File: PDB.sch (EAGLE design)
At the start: 53 parts, among them J1 B06B-HCMKK, J2 B06B-HCMKK, J3 SS-6488-NF-A431, J4 SS-6488-NF-A431, J5 B06B-HCMKK, J6 B03B-HCMKS, J7 B03B-HCMKS, J8 SS-6488-NF-A431

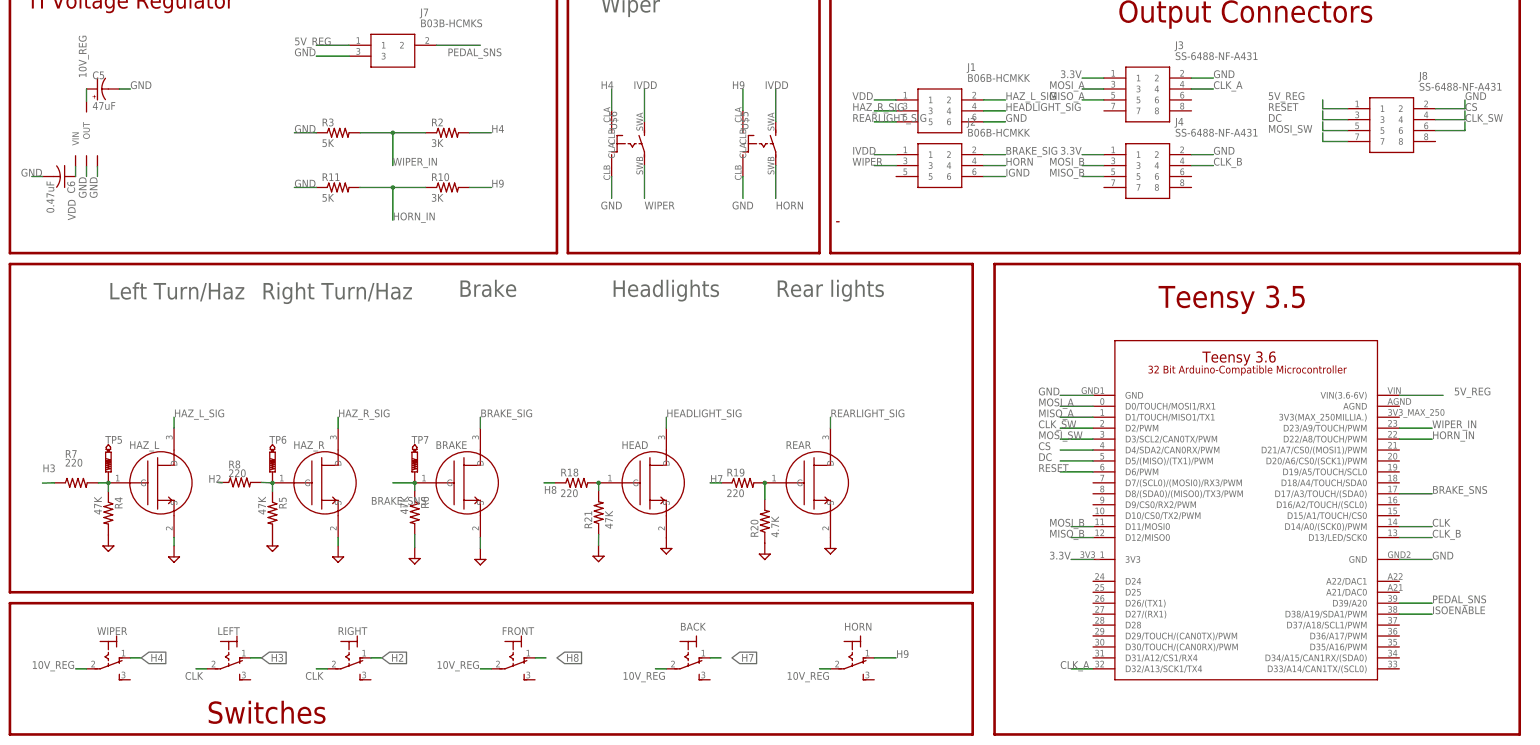
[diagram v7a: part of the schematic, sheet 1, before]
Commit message: With diode, pass signal direcely to ISOENABLE
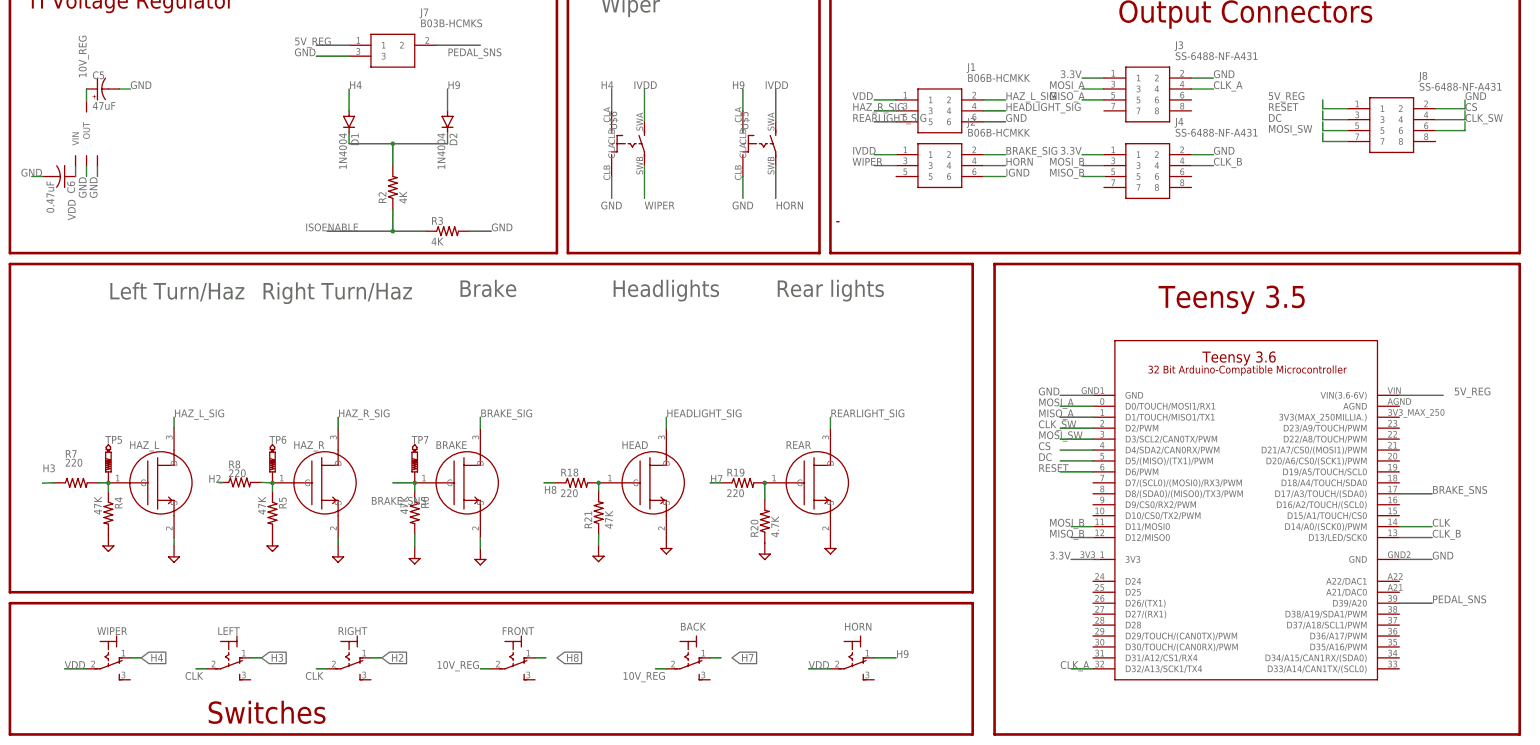
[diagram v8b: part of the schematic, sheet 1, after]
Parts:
- removed R10: 3K, master_library:R-US_R0805
- removed R11: 5K, master_library:R-US_R0805
- added D1, D2: 1N4004, diode:1N4004
- R2: value 3K -> 4K
- R3: value 5K -> 4K
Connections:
- removed net HORN_IN: R10.1, R11.2, U$3.D22/A8/TOUCH/PWM
- removed net WIPER_IN: R2.1, R3.2, U$3.D23/A9/TOUCH/PWM
- new net N$3: D1.C, D2.C, R2.2
- net 10V_REG: no longer HORN.P, WIPER.P
- net GND: now also R3.2; no longer R11.1, R3.1
- net H4: now also D1.A; no longer R2.2
- net H9: now also D2.A; no longer R10.2
- net ISOENABLE: now also R2.1, R3.1; no longer U$3.D38/A19/SDA1/PWM
- net VDD: now also HORN.P, WIPER.P
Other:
- moved on the sheet: R2, R3
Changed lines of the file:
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@@
 <part name="U$6" library="AUX Lib" deviceset="TE_CON_OJE-SH-112DM,095\" device=""/>
 <part name="J8" library="AUX Lib" deviceset="SS-6488-NF-A431" device=""/>
-<part name="R2" library="master_library" deviceset="R-US_" device="R0805" package3d_urn="urn:adsk.eagle:package:2274104/1" value="3K"/>
-<part name="R3" library="master_library" deviceset="R-US_" device="R0805" package3d_urn="urn:adsk.eagle:package:2274104/1" value="5K"/>
-<part name="R10" library="master_library" deviceset="R-US_" device="R0805" package3d_urn="urn:adsk.eagle:package:2274104/1" value="3K"/>
-<part name="R11" library="master_library" deviceset="R-US_" device="R0805" package3d_urn="urn:adsk.eagle:package:2274104/1" value="5K"/>
+<part name="D1" library="diode" library_urn="urn:adsk.eagle:library:210" deviceset="1N4004" device="" package3d_urn="urn:adsk.eagle:package:43336/1"/>
+<part name="D2" library="diode" library_urn="urn:adsk.eagle:library:210" deviceset="1N4004" device="" package3d_urn="urn:adsk.eagle:package:43336/1"/>
+<part name="R2" library="master_library" deviceset="R-US_" device="R0805" package3d_urn="urn:adsk.eagle:package:2274104/1" value="4K"/>
+<part name="R3" library="master_library" deviceset="R-US_" device="R0805" package3d_urn="urn:adsk.eagle:package:2274104/1" value="4K"/>
 </parts>
 <sheets>
@@
 <attribute name="VALUE" x="223.012" y="119.888" size="1.778" layer="96" align="center-left"/>
 </instance>
-<instance part="R2" gate="G$1" x="-2.54" y="109.22" smashed="yes">
-<attribute name="NAME" x="-6.35" y="110.7186" size="1.778" layer="95"/>
-<attribute name="VALUE" x="-6.35" y="105.918" size="1.778" layer="96"/>
-</instance>
-<instance part="R3" gate="G$1" x="-27.94" y="109.22" smashed="yes">
-<attribute name="NAME" x="-31.75" y="110.7186" size="1.778" layer="95"/>
-<attribute name="VALUE" x="-31.75" y="105.918" size="1.778" layer="96"/>
-</instance>
-<instance part="R10" gate="G$1" x="-2.54" y="96.52" smashed="yes">
-<attribute name="NAME" x="-6.35" y="98.0186" size="1.778" layer="95"/>
-<attribute name="VALUE" x="-6.35" y="93.218" size="1.778" layer="96"/>
-</instance>
-<instance part="R11" gate="G$1" x="-27.94" y="96.52" smashed="yes">
-<attribute name="NAME" x="-31.75" y="98.0186" size="1.778" layer="95"/>
-<attribute name="VALUE" x="-31.75" y="93.218" size="1.778" layer="96"/>
+<instance part="D1" gate="1" x="-25.4" y="111.76" smashed="yes" rot="R270">
+<attribute name="NAME" x="-24.9174" y="109.22" size="1.778" layer="95" rot="R270"/>
+<attribute name="VALUE" x="-27.7114" y="109.22" size="1.778" layer="96" rot="R270"/>
+</instance>
+<instance part="D2" gate="1" x="-2.54" y="111.76" smashed="yes" rot="R270">
+<attribute name="NAME" x="-2.0574" y="109.22" size="1.778" layer="95" rot="R270"/>
+<attribute name="VALUE" x="-4.8514" y="109.22" size="1.778" layer="96" rot="R270"/>
+</instance>
+<instance part="R2" gate="G$1" x="-15.24" y="96.52" smashed="yes" rot="R90">
+<attribute name="NAME" x="-16.7386" y="92.71" size="1.778" layer="95" rot="R90"/>
+<attribute name="VALUE" x="-11.938" y="92.71" size="1.778" layer="96" rot="R90"/>
+</instance>
+<instance part="R3" gate="G$1" x="-2.54" y="86.36" smashed="yes">
+<attribute name="NAME" x="-6.35" y="87.8586" size="1.778" layer="95"/>
+<attribute name="VALUE" x="-6.35" y="83.058" size="1.778" layer="96"/>
 </instance>
 </instances>
@@
 <label x="91.44" y="116.84" size="1.778" layer="95"/>
 </segment>
+<segment>
+<pinref part="WIPER" gate="1" pin="P"/>
+<wire x1="-86.36" y1="-15.24" x2="-91.44" y2="-15.24" width="0.1524" layer="91"/>
+<label x="-91.44" y="-15.24" size="1.778" layer="95"/>
+</segment>
+<segment>
+<pinref part="HORN" gate="1" pin="P"/>
+<wire x1="86.36" y1="-15.24" x2="81.28" y2="-15.24" width="0.1524" layer="91"/>
+<label x="81.28" y="-15.24" size="1.778" layer="95"/>
+</segment>
 </net>
 <net name="HAZ_L_SIG" class="0">
@@
 </segment>
 <segment>
-<pinref part="R2" gate="G$1" pin="2"/>
-<wire x1="2.54" y1="109.22" x2="7.62" y2="109.22" width="0.1524" layer="91"/>
-<label x="7.62" y="109.22" size="1.778" layer="95"/>
+<pinref part="D1" gate="1" pin="A"/>
+<wire x1="-25.4" y1="114.3" x2="-25.4" y2="119.38" width="0.1524" layer="91"/>
+<label x="-25.4" y="119.38" size="1.778" layer="95"/>
 </segment>
 </net>
@@
 </segment>
 <segment>
-<pinref part="WIPER" gate="1" pin="P"/>
-<wire x1="-86.36" y1="-15.24" x2="-88.9" y2="-15.24" width="0.1524" layer="91"/>
-<label x="-99.06" y="-15.24" size="1.778" layer="95"/>
-</segment>
-<segment>
 <pinref part="FRONT" gate="1" pin="P"/>
 <wire x1="7.62" y1="-15.24" x2="5.08" y2="-15.24" width="0.1524" layer="91"/>
@@
 <wire x1="48.26" y1="-15.24" x2="45.72" y2="-15.24" width="0.1524" layer="91"/>
 <label x="38.1" y="-17.78" size="1.778" layer="95"/>
-</segment>
-<segment>
-<pinref part="HORN" gate="1" pin="P"/>
-<wire x1="86.36" y1="-15.24" x2="83.82" y2="-15.24" width="0.1524" layer="91"/>
-<label x="76.2" y="-17.78" size="1.778" layer="95"/>
 </segment>
 </net>
@@
 </segment>
 <segment>
-<pinref part="R3" gate="G$1" pin="1"/>
-<wire x1="-33.02" y1="109.22" x2="-38.1" y2="109.22" width="0.1524" layer="91"/>
-<label x="-38.1" y="109.22" size="1.778" layer="95"/>
-</segment>
-<segment>
-<pinref part="R11" gate="G$1" pin="1"/>
-<wire x1="-33.02" y1="96.52" x2="-38.1" y2="96.52" width="0.1524" layer="91"/>
-<label x="-38.1" y="96.52" size="1.778" layer="95"/>
+<pinref part="R3" gate="G$1" pin="2"/>
+<wire x1="2.54" y1="86.36" x2="7.62" y2="86.36" width="0.1524" layer="91"/>
+<label x="7.62" y="86.36" size="1.778" layer="95"/>
 </segment>
 </net>
@@
 </segment>
 <segment>
-<pinref part="U$3" gate="G$1" pin="D38/A19/SDA1/PWM"/>
-<wire x1="218.44" y1="-2.54" x2="226.06" y2="-2.54" width="0.1524" layer="91"/>
-<label x="226.06" y="-2.54" size="1.778" layer="95"/>
+<pinref part="R2" gate="G$1" pin="1"/>
+<wire x1="-15.24" y1="91.44" x2="-15.24" y2="86.36" width="0.1524" layer="91"/>
+<wire x1="-15.24" y1="86.36" x2="-7.62" y2="86.36" width="0.1524" layer="91"/>
+<pinref part="R3" gate="G$1" pin="1"/>
+<wire x1="-15.24" y1="86.36" x2="-30.48" y2="86.36" width="0.1524" layer="91"/>
+<junction x="-15.24" y="86.36"/>
+<label x="-35.56" y="86.36" size="1.778" layer="95"/>
 </segment>
 </net>
@@
 </segment>
 <segment>
-<pinref part="R10" gate="G$1" pin="2"/>
-<wire x1="2.54" y1="96.52" x2="7.62" y2="96.52" width="0.1524" layer="91"/>
-<label x="7.62" y="96.52" size="1.778" layer="95"/>
+<pinref part="D2" gate="1" pin="A"/>
+<wire x1="-2.54" y1="114.3" x2="-2.54" y2="119.38" width="0.1524" layer="91"/>
+<label x="-2.54" y="119.38" size="1.778" layer="95"/>
 </segment>
 </net>
@@
 </segment>
 </net>
-<net name="WIPER_IN" class="0">
-<segment>
-<pinref part="U$3" gate="G$1" pin="D23/A9/TOUCH/PWM"/>
-<wire x1="218.44" y1="40.64" x2="226.06" y2="40.64" width="0.1524" layer="91"/>
-<label x="226.06" y="40.64" size="1.778" layer="95"/>
-</segment>
-<segment>
-<pinref part="R2" gate="G$1" pin="1"/>
-<pinref part="R3" gate="G$1" pin="2"/>
-<wire x1="-7.62" y1="109.22" x2="-15.24" y2="109.22" width="0.1524" layer="91"/>
-<wire x1="-15.24" y1="109.22" x2="-22.86" y2="109.22" width="0.1524" layer="91"/>
-<wire x1="-15.24" y1="109.22" x2="-15.24" y2="101.6" width="0.1524" layer="91"/>
-<junction x="-15.24" y="109.22"/>
-<label x="-15.24" y="101.6" size="1.778" layer="95"/>
-</segment>
-</net>
-<net name="HORN_IN" class="0">
-<segment>
-<pinref part="U$3" gate="G$1" pin="D22/A8/TOUCH/PWM"/>
-<wire x1="218.44" y1="38.1" x2="226.06" y2="38.1" width="0.1524" layer="91"/>
-<label x="226.06" y="38.1" size="1.778" layer="95"/>
-</segment>
-<segment>
-<pinref part="R10" gate="G$1" pin="1"/>
-<pinref part="R11" gate="G$1" pin="2"/>
-<wire x1="-7.62" y1="96.52" x2="-15.24" y2="96.52" width="0.1524" layer="91"/>
-<wire x1="-15.24" y1="96.52" x2="-22.86" y2="96.52" width="0.1524" layer="91"/>
-<wire x1="-15.24" y1="96.52" x2="-15.24" y2="88.9" width="0.1524" layer="91"/>
-<junction x="-15.24" y="96.52"/>
-<label x="-15.24" y="88.9" size="1.778" layer="95"/>
-</segment>
-</net>
+<net name="N$3" class="0">
+<segment>
+<pinref part="D2" gate="1" pin="C"/>
+<wire x1="-2.54" y1="109.22" x2="-2.54" y2="106.68" width="0.1524" layer="91"/>
+<pinref part="D1" gate="1" pin="C"/>
+<wire x1="-25.4" y1="109.22" x2="-25.4" y2="106.68" width="0.1524" layer="91"/>
+<wire x1="-2.54" y1="106.68" x2="-15.24" y2="106.68" width="0.1524" layer="91"/>
+<wire x1="-15.24" y1="106.68" x2="-25.4" y2="106.68" width="0.1524" layer="91"/>
+<wire x1="-15.24" y1="106.68" x2="-15.24" y2="101.6" width="0.1524" layer="91"/>
+<junction x="-15.24" y="106.68"/>
+<pinref part="R2" gate="G$1" pin="2"/>
+</segment>
+</net>
